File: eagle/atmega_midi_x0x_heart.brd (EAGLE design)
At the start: 100 x 80 mm, 40 parts, among them J11_VCF_CUTOFF 22-23-2021, U1 ATMEGA328P_PDIP, U2 TLV2372IP

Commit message: brd drc
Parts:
- moved PWR1 6.48 mm to (14.0, 27.9)
- moved RES1 2.54 mm to (87.6, 17.8)
- moved RES2 2.54 mm to (69.8, 17.8)
- moved U$1 2.54 mm to (82.5, 15.2)
- moved C8 1.27 mm to (12.7, 64.8)
- moved RST2 1.27 mm to (24.1, 35.6)
- turned C5 to 0 degrees

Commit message: layout tweaks
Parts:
- moved R9 13.7 mm to (44.5, 29.2)
- moved MIDI_OUT_THRU 9.25 mm to (38.1, 22.9), turned to 270 degrees
- moved J2_SEQ 9.16 mm to (71.1, 58.4)
- moved OK1 7.62 mm to (30.5, 24.1)
- moved R2 7.62 mm to (30.5, 16.5)
- moved R3 7.62 mm to (22.9, 24.1), turned to 90 degrees
- moved R5 6.48 mm to (38.1, 59.7)
- moved D1 6.35 mm to (30.5, 12.7)
- moved MIDI_IN 5.24 mm to (40.6, 14.0)
- moved C1 3.59 mm to (53.3, 25.4), turned to 270 degrees
- moved MIDI_CH 2.84 mm to (54.6, 52.1), turned to 270 degrees
- moved R10 2.84 mm to (31.8, 72.4)
- moved SCALE_TRIM 2.84 mm to (34.3, 66.0), turned to 90 degrees
- moved J3_VOICE 2.54 mm to (78.7, 43.2)
- moved Q1 2.54 mm to (61.0, 29.2)
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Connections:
- net N$37: now also U$1.2; no longer U$1.3
- net N$41: now also U$1.3; no longer U$1.2

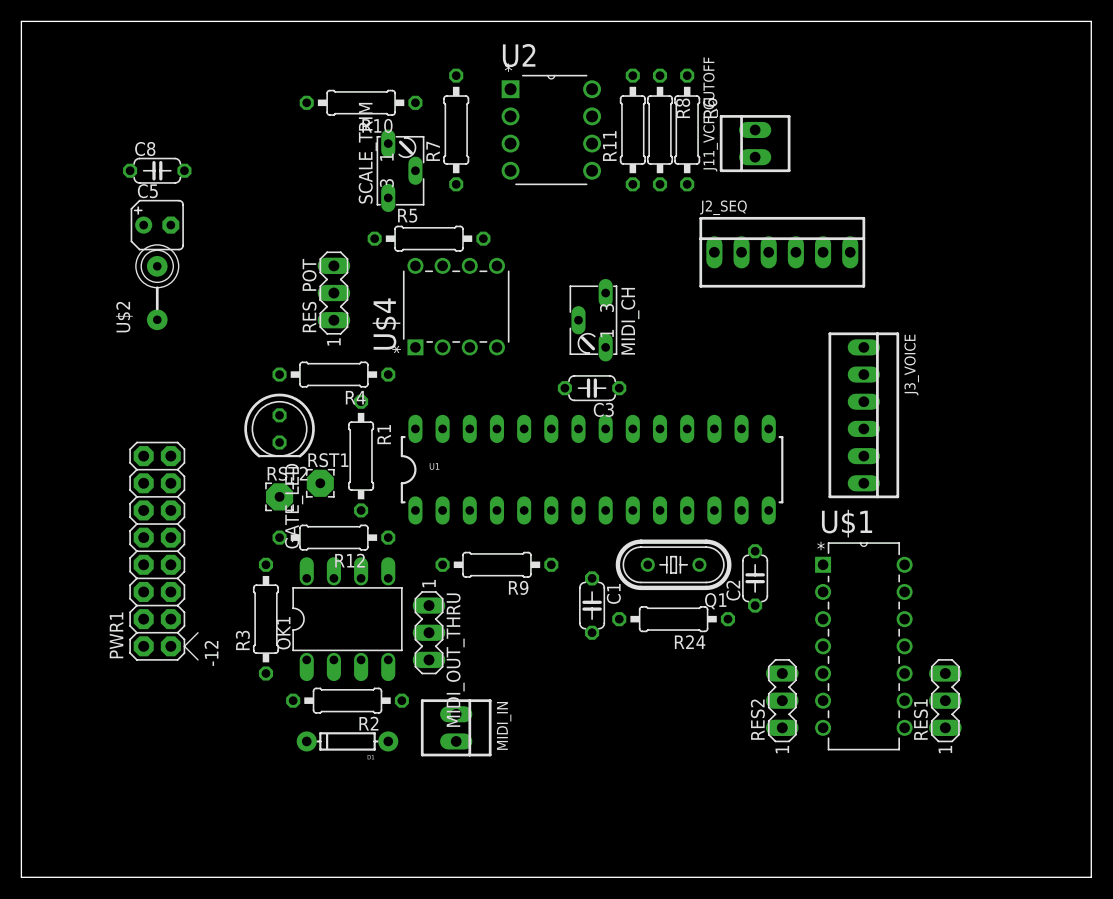
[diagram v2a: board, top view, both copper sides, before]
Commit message: 97 pct autorouted
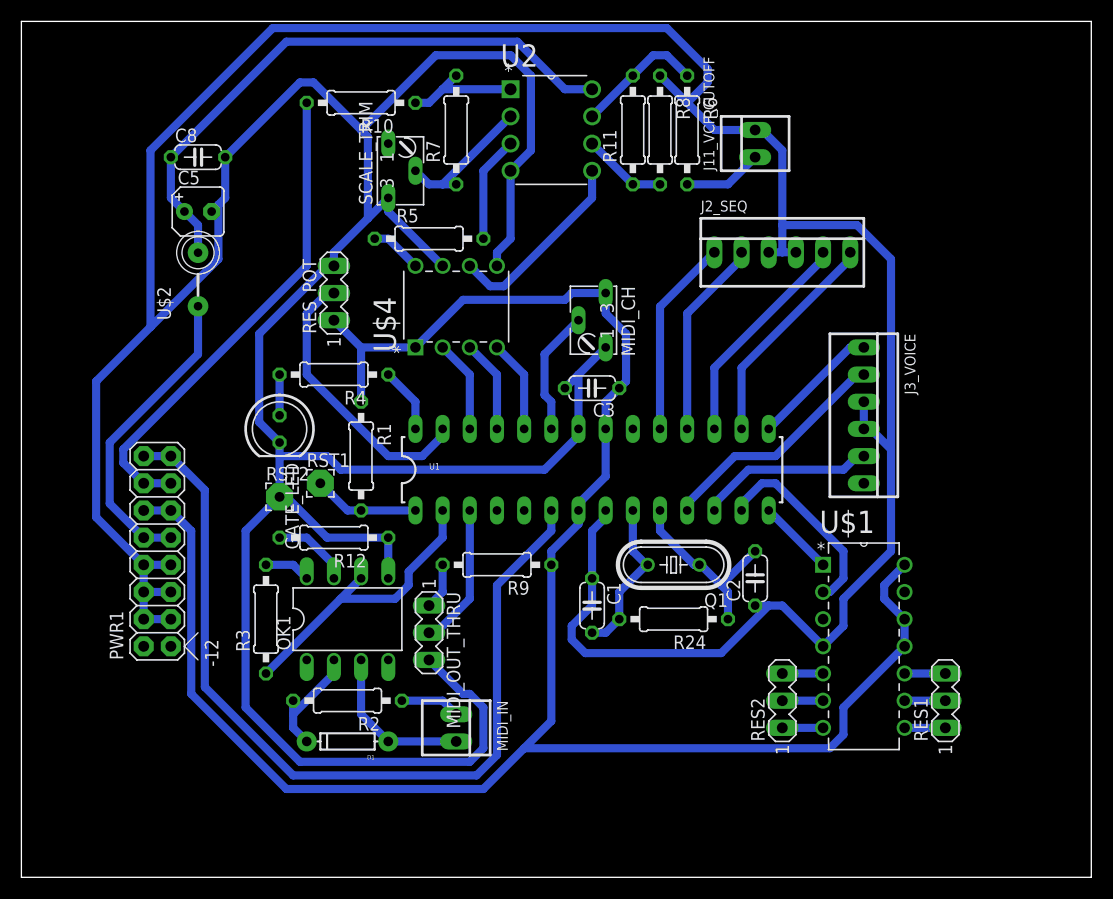
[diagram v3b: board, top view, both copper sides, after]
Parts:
- moved U$2 4.02 mm to (16.5, 55.9)
- moved C5 4.02 mm to (16.5, 62.2)
- moved C8 4.02 mm to (16.5, 67.3)
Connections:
- net N$10: now also U1.11; no longer U1.12
- net N$16: now also U1.12; no longer U1.11
- net N$37: now also U$1.1; no longer U$1.2
- net N$40: now also U$1.3; no longer U$1.1
- net N$41: now also U$1.2; no longer U$1.3
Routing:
- net GND: track 0.00 -> 482.7 mm
- net +5V: track 0.00 -> 192.3 mm
- net N$22: track 0.00 -> 81.9 mm
- net +12V: track 0.00 -> 55.7 mm
- net N$15: track 0.00 -> 46.0 mm
- net N$11: track 0.00 -> 28.9 mm
- net N$30: track 0.00 -> 27.7 mm
- net N$38: track 0.00 -> 26.3 mm
- net N$10: track 0.00 -> 22.1 mm
- net N$21: track 0.00 -> 20.7 mm
- net N$23: track 0.00 -> 20.7 mm
- net N$20: track 0.00 -> 18.6 mm
- net N$18: track 0.00 -> 18.6 mm
- net N$41: track 0.00 -> 18.6 mm
- net N$14: track 0.00 -> 18.2 mm
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
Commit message: switched gate and pot ctrl pins for positioning
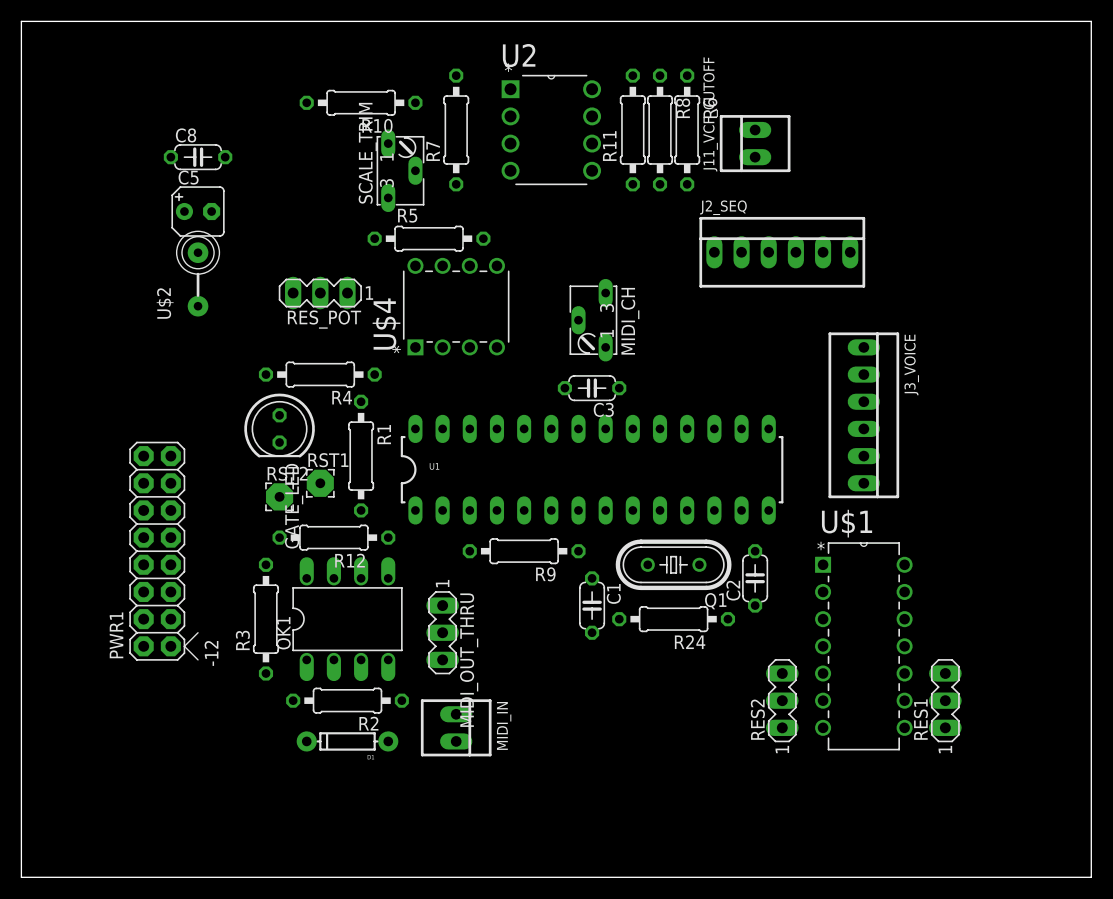
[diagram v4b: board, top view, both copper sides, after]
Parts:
- moved R9 2.84 mm to (47.0, 30.5)
- moved R4 1.27 mm to (27.9, 47.0)
- moved RES_POT 1.27 mm to (27.9, 54.6), turned to 180 degrees
- moved MIDI_OUT_THRU 1.27 mm to (39.4, 22.9)
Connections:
- net N$22: now also U$1.3; no longer PWR1.15, PWR1.16
- net N$40: now also PWR1.15, PWR1.16; no longer U$1.3
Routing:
- net GND: track 482.7 -> 0.00 mm
- net +5V: track 192.3 -> 0.00 mm
- net N$22: track 81.9 -> 0.00 mm
- net +12V: track 55.7 -> 0.00 mm
- net N$15: track 46.0 -> 0.00 mm
- net N$11: track 28.9 -> 0.00 mm
- net N$30: track 27.7 -> 0.00 mm
- net N$38: track 26.3 -> 0.00 mm
- net N$10: track 22.1 -> 0.00 mm
- net N$21: track 20.7 -> 0.00 mm
- net N$23: track 20.7 -> 0.00 mm
- net N$20: track 18.6 -> 0.00 mm
- net N$18: track 18.6 -> 0.00 mm
- net N$41: track 18.6 -> 0.00 mm
- net N$14: track 18.2 -> 0.00 mm
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
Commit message: almost
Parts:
- moved C8 7.62 mm to (16.5, 59.7)
- moved RES2 7.18 mm to (66.0, 11.4), turned to 180 degrees
- moved R6 6.84 mm to (59.7, 63.5), turned to 90 degrees
- moved U$2 6.35 mm to (12.7, 50.8), turned to 0 degrees
- moved C5 6.35 mm to (16.5, 55.9)
- moved U2 5.68 mm to (50.8, 61.0)
- moved R11 4.58 mm to (54.6, 66.0)
- moved R8 4.58 mm to (57.1, 66.0)
- moved SCALE_TRIM 4.02 mm to (33.0, 62.2), turned to 180 degrees
- moved R2 4.02 mm to (29.2, 12.7)
- moved C2 4.02 mm to (67.3, 24.1)
- moved D1 4.02 mm to (29.2, 8.89)
- moved OK1 4.02 mm to (29.2, 20.3)
- moved R3 4.02 mm to (21.6, 20.3)
- moved PWR1 3.81 mm to (12.7, 24.1)
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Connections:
- new net N$46: U1.21
- net +5V: no longer U1.21
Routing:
- net GND: track 0.00 -> 388.1 mm
- net +5V: track 0.00 -> 147.3 mm
- net N$1: track 0.00 -> 91.4 mm
- net N$22: track 0.00 -> 90.1 mm
- net N$30: track 0.00 -> 65.7 mm
- net +12V: track 0.00 -> 54.8 mm
- net N$40: track 0.00 -> 49.3 mm
- net N$15: track 0.00 -> 49.1 mm
- net N$11: track 0.00 -> 28.7 mm
- net N$10: track 0.00 -> 24.5 mm
- net N$21: track 0.00 -> 20.9 mm
- net N$23: track 0.00 -> 20.8 mm
- net N$17: track 0.00 -> 19.3 mm
- net N$20: track 0.00 -> 18.8 mm
- net N$38: track 0.00 -> 18.7 mm
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
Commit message: routed
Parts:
- moved RST1 1.70 mm to (27.4, 35.3)
- moved C8 1.05 mm to (17.5, 59.9)
- moved R7 1.02 mm to (38.7, 66.3)
- moved R4 0.76 mm to (25.9, 44.5)
- moved U$2 0.76 mm to (12.7, 51.6)
- moved R3 0.64 mm to (21.0, 20.3)
- moved C1 0.25 mm to (52.3, 22.9)
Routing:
- net +5V: track 147.3 -> 191.6 mm, vias 0 -> 4
- net N$30: track 65.7 -> 70.0 mm
- net N$40: track 49.3 -> 53.5 mm
- net N$1: track 91.4 -> 94.6 mm
- net N$22: track 90.1 -> 93.3 mm
- net +12V: track 54.8 -> 51.9 mm
- net N$12: track 13.2 -> 16.0 mm
- net GND: track 388.1 -> 389.9 mm
- net N$27: track 10.6 -> 8.99 mm
- net N$43: track 11.7 -> 10.2 mm
- net N$20: track 18.8 -> 17.6 mm
- net N$38: track 18.7 -> 19.9 mm
- net N$11: track 28.7 -> 29.8 mm
- net N$42: track 13.8 -> 14.8 mm
- net N$18: track 18.7 -> 17.8 mm
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
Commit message: cutout
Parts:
- moved RES2 4.49 mm to (69.1, 14.7), turned to 90 degrees
- moved RES1 1.52 mm to (85.1, 15.5)
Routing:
- net N$36: track 13.4 -> 5.85 mm
- net N$34: track 10.2 -> 5.59 mm
- net +5V: track 191.6 -> 190.4 mm
- net N$22: track 93.3 -> 92.2 mm
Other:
- outline, holes or cut-outs redrawn

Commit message: ds1267 is there
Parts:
- added C4, C7: 10u, rcl:B45181A
- added C6: 100n, rcl:C050-024X044
- added D2: 5V, diode:DO34Z7
- added R13: 100, rcl:0207/10
- added U3: DS1267S-010+DIP14, Maxim_By_element14_Batch_1:DIP14
- U$1: value MCP42050-E/P -> FB; device MCP42050-E_P:DIP254P762X432-14 -> adafruit:FB
- moved U$1 61.0 mm to (20.3, 12.7), turned to 270 degrees
- moved R11 12.5 mm to (43.2, 71.1), turned to 180 degrees
- moved U2 8.52 mm to (47.0, 68.6), turned to 90 degrees
- moved R4 7.41 mm to (19.6, 48.3)
- moved SCALE_TRIM 5.24 mm to (27.9, 63.5)
- moved R7 5.24 mm to (33.7, 67.6)
- moved R10 5.08 mm to (25.4, 69.8)
- moved MIDI_CH 5.08 mm to (53.3, 54.6)
- moved R1 5.08 mm to (30.5, 41.9)
- moved GATE_LED 4.02 mm to (21.6, 43.2)
- moved RST2 4.02 mm to (22.9, 38.1)
- moved D1 4.02 mm to (27.9, 12.7)
- moved R12 3.81 mm to (26.7, 33.0)
- moved R2 3.81 mm to (29.2, 16.5)
- moved MIDI_IN 3.81 mm to (39.4, 15.2)
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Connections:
- new net -12V: C4.-, C6.2, R13.1, U$1.P$2
- new net N$47: PWR1.1, PWR1.2, U$1.P$1
- new net N$49: C7.-, D2.A, R13.2, U3.1
- net +5V: now also U3.14; no longer U$1.11, U$1.12, U$1.14
- net GND: now also C4.+, C6.1, C7.+, D2.C, U3.7; no longer U$1.4
- net N$22: now also U3.5; no longer U$1.3
- net N$31: now also U3.4; no longer U$1.9
- net N$32: now also U3.2; no longer U$1.8
- net N$33: now also U3.3; no longer U$1.10
- net N$34: now also U3.12; no longer U$1.6
- net N$35: now also U3.11; no longer U$1.7
- net N$36: now also U3.10; no longer U$1.5
- net N$37: now also U3.6; no longer U$1.1
- net N$41: now also U3.8; no longer U$1.2
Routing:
- net GND: track 389.9 -> 0.00 mm
- net +5V: track 190.4 -> 0.00 mm, vias 4 -> 0
- net N$1: track 94.9 -> 0.00 mm
- net N$22: track 92.2 -> 0.00 mm
- net N$30: track 70.0 -> 0.00 mm
- net N$40: track 53.5 -> 0.00 mm
- net +12V: track 51.9 -> 0.00 mm
- net N$15: track 49.1 -> 0.00 mm
- net N$11: track 29.8 -> 0.00 mm
- net N$10: track 24.5 -> 0.00 mm
- net N$23: track 20.1 -> 0.00 mm
- net N$21: track 20.0 -> 0.00 mm
- net N$38: track 19.9 -> 0.00 mm
- net N$17: track 19.6 -> 0.00 mm
- net N$18: track 17.8 -> 0.00 mm
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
